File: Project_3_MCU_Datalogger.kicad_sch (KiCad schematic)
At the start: 25 parts, among them U1 24LC1025, U2 24LC1025, U3 DS1337S_, U4 ATMEGA328P-AU, Y1 Crystal, Y2 Crystal

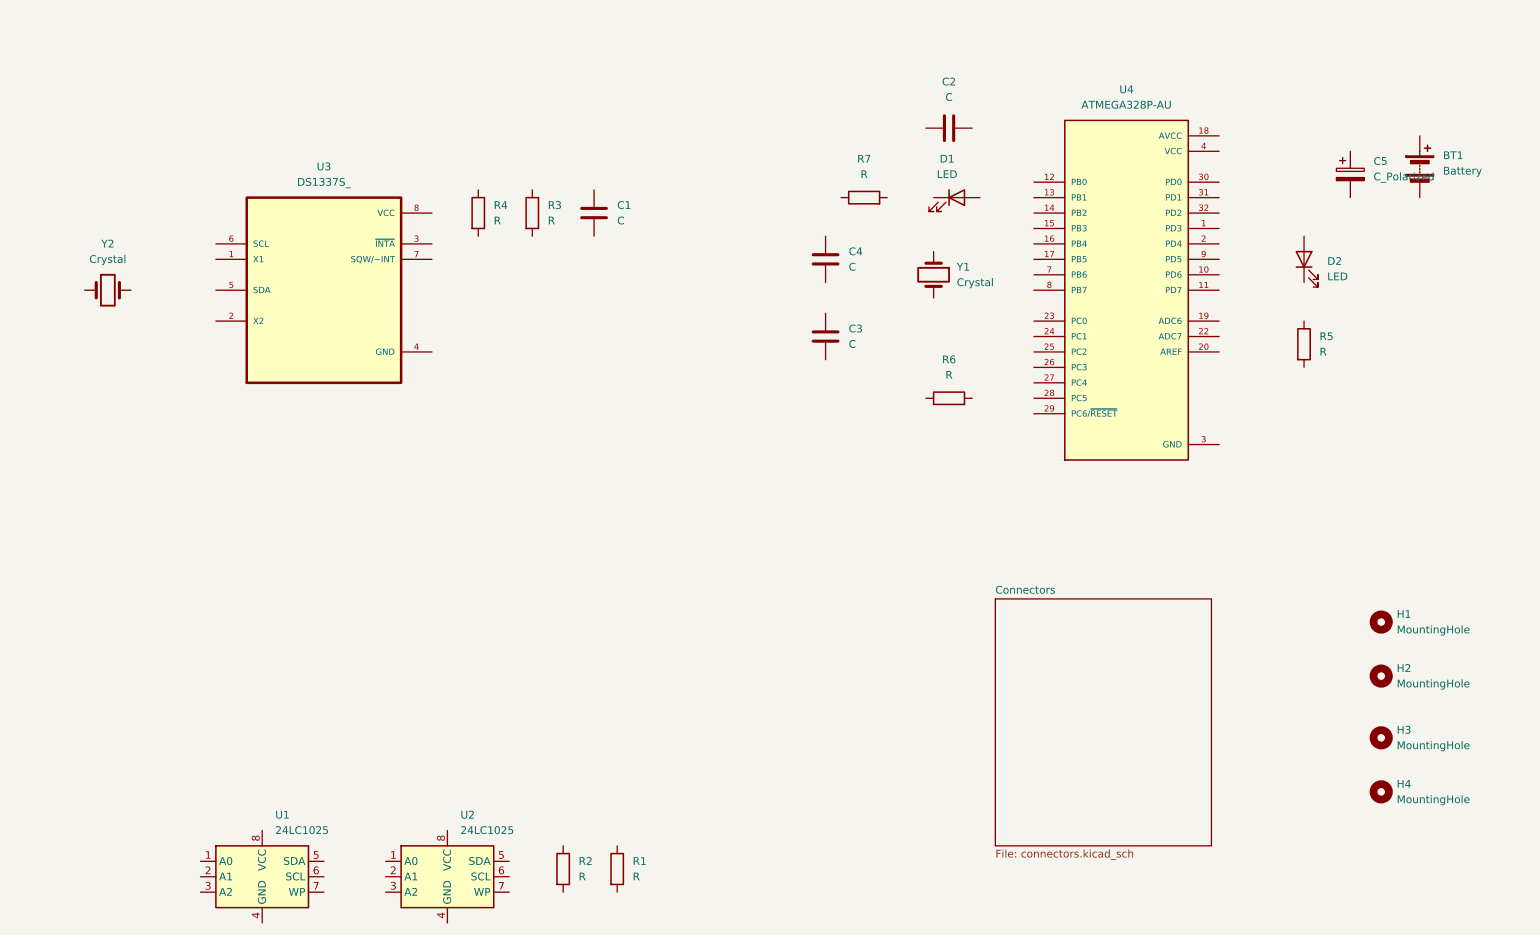
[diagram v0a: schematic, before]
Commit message: ajout des valeurs de composants
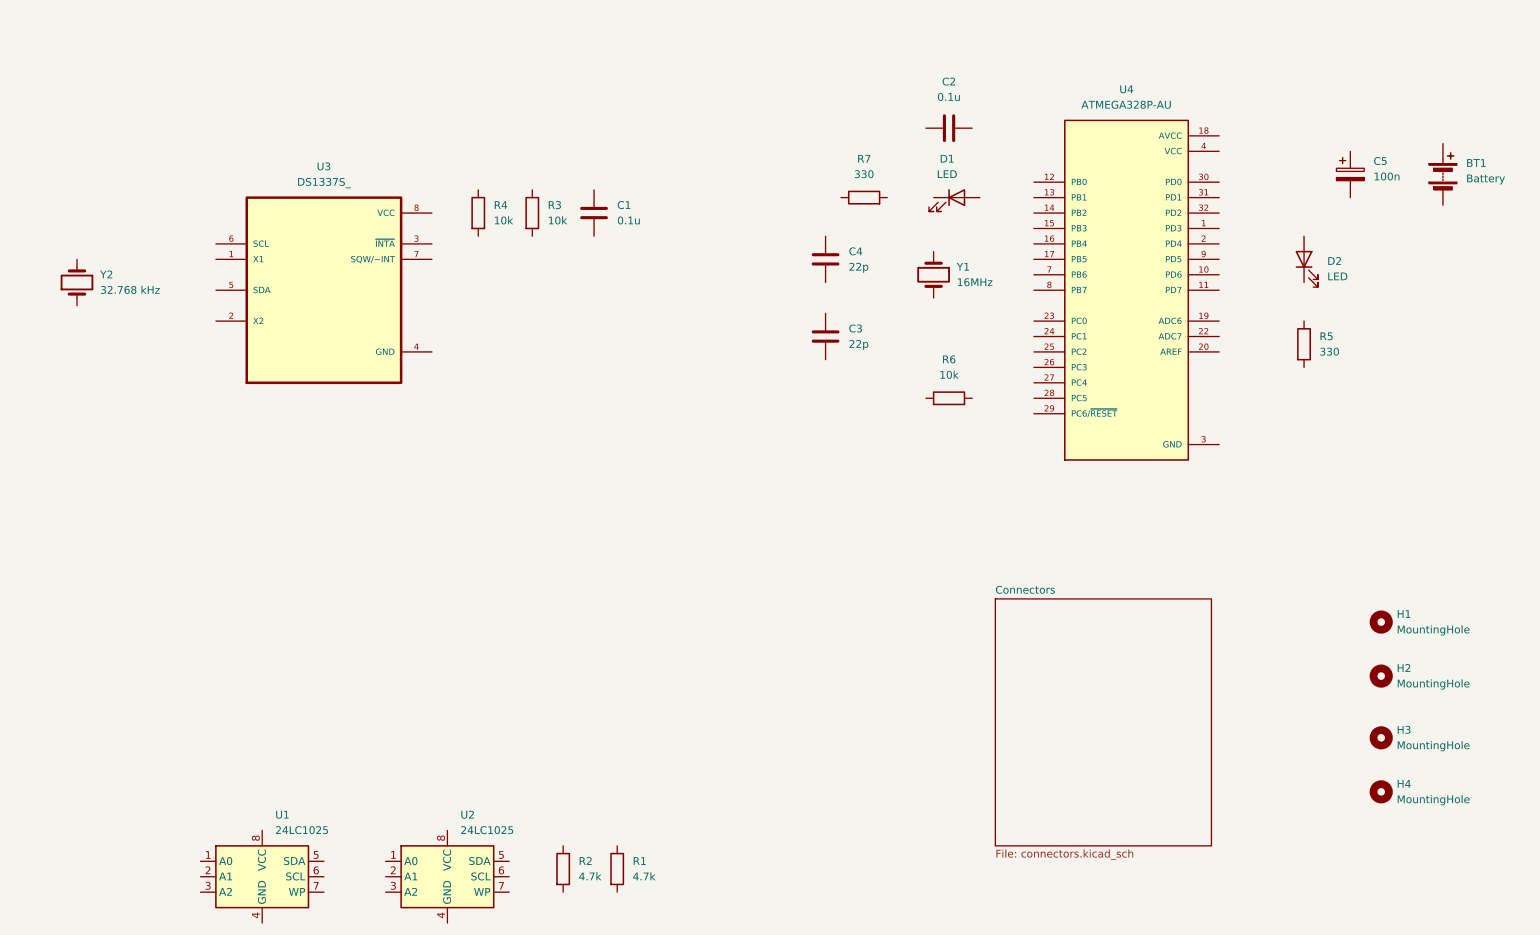
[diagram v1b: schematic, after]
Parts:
- C1, C2: value C -> 0.1u
- C3, C4: value C -> 22p
- C5: value C_Polarized -> 100n
- R1, R2: value R -> 4.7k
- R3, R4, R6: value R -> 10k
- R5, R7: value R -> 330
- Y1: value Crystal -> 16MHz
- Y2: value Crystal -> 32.768 kHz
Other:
- moved on the sheet: BT1, Y2
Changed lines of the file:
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@@
 			)
 		)
-		(property "Value" "Crystal"
+		(property "Value" "16MHz"
 			(at 180.34 66.0399 90)
 			(show_name no)
@@
 			)
 		)
-		(property "Value" "C"
+		(property "Value" "0.1u"
 			(at 124.46 55.8799 0)
 			(show_name no)
@@
 			)
 		)
-		(property "Value" "R"
+		(property "Value" "4.7k"
 			(at 118.11 163.8299 0)
 			(show_name no)
@@
 			)
 		)
-		(property "Value" "R"
+		(property "Value" "4.7k"
 			(at 127 163.8299 0)
 			(show_name no)
@@
 	(symbol
 		(lib_id "Device:Crystal")
-		(at 40.64 67.31 0)
+		(at 35.56 66.04 90)
 		(unit 1)
 		(body_style 1)
@@
 		(fields_autoplaced yes)
 		(property "Reference" "Y2"
-			(at 40.64 59.69 0)
-			(show_name no)
-			(do_not_autoplace no)
-			(effects
-				(font
-					(size 1.27 1.27)
-				)
-			)
-		)
-		(property "Value" "Crystal"
-			(at 40.64 62.23 0)
-			(show_name no)
-			(do_not_autoplace no)
-			(effects
-				(font
-					(size 1.27 1.27)
-				)
+			(at 39.37 64.7699 90)
+			(show_name no)
+			(do_not_autoplace no)
+			(effects
+				(font
+					(size 1.27 1.27)
+				)
+				(justify right)
+			)
+		)
+		(property "Value" "32.768 kHz"
+			(at 39.37 67.3099 90)
+			(show_name no)
+			(do_not_autoplace no)
+			(effects
+				(font
+					(size 1.27 1.27)
+				)
+				(justify right)
 			)
 		)
 		(property "Footprint" ""
-			(at 40.64 67.31 0)
+			(at 35.56 66.04 0)
 			(hide yes)
 			(show_name no)
@@
 		)
 		(property "Datasheet" ""
-			(at 40.64 67.31 0)
+			(at 35.56 66.04 0)
 			(hide yes)
 			(show_name no)
@@
 		)
 		(property "Description" "Two pin crystal"
-			(at 40.64 67.31 0)
-			(hide yes)
+			(at 35.56 66.04 0)
+			(hide yes)
+			(show_name no)
+			(do_not_autoplace no)
+			(effects
+				(font
+					(size 1.27 1.27)
+				)
+			)
+		)
+		(property "Purpose" ""
+			(at 35.56 66.04 0)
 			(show_name no)
 			(do_not_autoplace no)
@@
 			)
 		)
-		(property "Value" "R"
+		(property "Value" "10k"
 			(at 179.07 81.28 90)
 			(show_name no)
@@
 			)
 		)
-		(property "Value" "C"
+		(property "Value" "22p"
 			(at 162.56 76.1999 0)
 			(show_name no)
@@
 			)
 		)
-		(property "Value" "C"
+		(property "Value" "0.1u"
 			(at 179.07 35.56 90)
 			(show_name no)
@@
 			)
 		)
-		(property "Value" "C_Polarized"
+		(property "Value" "100n"
 			(at 248.92 48.6409 0)
 			(show_name no)
@@
 			)
 		)
-		(property "Value" "C"
+		(property "Value" "22p"
 			(at 162.56 63.4999 0)
 			(show_name no)
@@
 			)
 		)
-		(property "Value" "R"
+		(property "Value" "330"
 			(at 240.03 77.4699 0)
 			(show_name no)
@@
 	(symbol
 		(lib_id "Device:Battery")
-		(at 256.54 46.99 0)
+		(at 260.35 48.26 0)
 		(unit 1)
 		(body_style 1)
@@
 		(fields_autoplaced yes)
 		(property "Reference" "BT1"
-			(at 260.35 45.1484 0)
+			(at 264.16 46.4184 0)
 			(show_name no)
 			(do_not_autoplace no)
@@
 		)
 		(property "Value" "Battery"
-			(at 260.35 47.6884 0)
+			(at 264.16 48.9584 0)
 			(show_name no)
 			(do_not_autoplace no)
@@
 		)
 		(property "Footprint" ""
-			(at 256.54 45.466 90)
+			(at 260.35 46.736 90)
 			(hide yes)
 			(show_name no)
@@
 		)
 		(property "Datasheet" ""
-			(at 256.54 45.466 90)
+			(at 260.35 46.736 90)
 			(hide yes)
 			(show_name no)
@@
 		)
 		(property "Description" "Multiple-cell battery"
-			(at 256.54 46.99 0)
+			(at 260.35 48.26 0)
 			(hide yes)
 			(show_name no)
@@
 		)
 		(property "Sim.Device" "V"
-			(at 256.54 46.99 0)
+			(at 260.35 48.26 0)
 			(hide yes)
 			(show_name no)
@@
 		)
 		(property "Sim.Type" "DC"
-			(at 256.54 46.99 0)
+			(at 260.35 48.26 0)
 			(hide yes)
 			(show_name no)
@@
 		)
 		(property "Sim.Pins" "1=+ 2=-"
-			(at 256.54 46.99 0)
+			(at 260.35 48.26 0)
 			(hide yes)
 			(show_name no)
@@
 			)
 		)
-		(property "Value" "R"
+		(property "Value" "10k"
 			(at 113.03 55.8799 0)
 			(show_name no)
@@
 			)
 		)
-		(property "Value" "R"
+		(property "Value" "10k"
 			(at 104.14 55.8799 0)
 			(show_name no)
@@
 			)
 		)
+		(property "Purpose" ""
+			(at 101.6 54.61 0)
+			(show_name no)
+			(do_not_autoplace no)
+			(effects
+				(font
+					(size 1.27 1.27)
+				)
+			)
+		)
 		(pin "2"
 		)
@@
 			)
 		)
-		(property "Value" "R"
+		(property "Value" "330"
 			(at 165.1 48.26 90)
 			(show_name no)

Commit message: Association des empreintes aux composants
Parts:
- BT1: footprint (none) -> Connector_PinHeader_2.54mm:PinHeader_1x02_P2.54mm_Vertical
- C1, C2, C3, C4, C5: footprint (none) -> Capacitor_SMD:C_0805_2012Metric
- D1, D2: footprint (none) -> LED_SMD:LED_0805_2012Metric
- H1, H2, H3, H4: footprint (none) -> MountingHole:MountingHole_2.1mm
- R1, R2, R3, R4, R5, R6, R7: footprint (none) -> Resistor_SMD:R_0805_2012Metric
- U1, U2: footprint (none) -> Package_SO:SOIC-8_5.3x5.3mm_P1.27mm
- Y1, Y2: footprint (none) -> Crystal:Crystal_SMD_5032-2Pin_5.0x3.2mm_HandSoldering
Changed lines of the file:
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@@
 			)
 		)
-		(property "Footprint" ""
+		(property "Footprint" "Crystal:Crystal_SMD_5032-2Pin_5.0x3.2mm_HandSoldering"
 			(at 176.53 64.77 0)
 			(hide yes)
@@
 			)
 		)
-		(property "Footprint" ""
+		(property "Footprint" "LED_SMD:LED_0805_2012Metric"
 			(at 180.34 52.07 0)
 			(hide yes)
@@
 			)
 		)
-		(property "Footprint" ""
+		(property "Footprint" "Capacitor_SMD:C_0805_2012Metric"
 			(at 121.6152 58.42 0)
 			(hide yes)
@@
 			)
 		)
-		(property "Footprint" ""
+		(property "Footprint" "Package_SO:SOIC-8_5.3x5.3mm_P1.27mm"
 			(at 96.52 163.83 0)
 			(hide yes)
@@
 			)
 		)
-		(property "Footprint" ""
+		(property "Footprint" "MountingHole:MountingHole_2.1mm"
 			(at 250.19 149.86 0)
 			(hide yes)
@@
 			)
 		)
-		(property "Footprint" ""
+		(property "Footprint" "MountingHole:MountingHole_2.1mm"
 			(at 250.19 130.81 0)
 			(hide yes)
@@
 			)
 		)
-		(property "Footprint" ""
+		(property "Footprint" "Resistor_SMD:R_0805_2012Metric"
 			(at 113.792 162.56 90)
 			(hide yes)
@@
 			)
 		)
-		(property "Footprint" ""
+		(property "Footprint" "Resistor_SMD:R_0805_2012Metric"
 			(at 122.682 162.56 90)
 			(hide yes)
@@
 			)
 		)
-		(property "Footprint" ""
+		(property "Footprint" "Crystal:Crystal_SMD_5032-2Pin_5.0x3.2mm_HandSoldering"
 			(at 35.56 66.04 0)
 			(hide yes)
@@
 			)
 		)
-		(property "Footprint" ""
+		(property "Footprint" "Resistor_SMD:R_0805_2012Metric"
 			(at 179.07 86.868 90)
 			(hide yes)
@@
 			)
 		)
-		(property "Footprint" ""
+		(property "Footprint" "Capacitor_SMD:C_0805_2012Metric"
 			(at 159.7152 78.74 0)
 			(hide yes)
@@
 			)
 		)
-		(property "Footprint" ""
+		(property "Footprint" "LED_SMD:LED_0805_2012Metric"
 			(at 237.49 62.23 0)
 			(hide yes)
@@
 			)
 		)
-		(property "Footprint" ""
+		(property "Footprint" "Capacitor_SMD:C_0805_2012Metric"
 			(at 182.88 39.6748 0)
 			(hide yes)
@@
 			)
 		)
-		(property "Footprint" ""
+		(property "Footprint" "Capacitor_SMD:C_0805_2012Metric"
 			(at 246.0752 52.07 0)
 			(hide yes)
@@
 			)
 		)
-		(property "Footprint" ""
+		(property "Footprint" "MountingHole:MountingHole_2.1mm"
 			(at 250.19 121.92 0)
 			(hide yes)
@@
 			)
 		)
-		(property "Footprint" ""
+		(property "Footprint" "Capacitor_SMD:C_0805_2012Metric"
 			(at 157.7848 58.42 0)
 			(hide yes)
@@
 			)
 		)
-		(property "Footprint" ""
+		(property "Footprint" "Resistor_SMD:R_0805_2012Metric"
 			(at 235.712 76.2 90)
 			(hide yes)
@@
 			)
 		)
-		(property "Footprint" ""
+		(property "Footprint" "Connector_PinHeader_2.54mm:PinHeader_1x02_P2.54mm_Vertical"
 			(at 260.35 46.736 90)
 			(hide yes)
@@
 			)
 		)
-		(property "Footprint" ""
+		(property "Footprint" "Resistor_SMD:R_0805_2012Metric"
 			(at 108.712 54.61 90)
 			(hide yes)
@@
 			)
 		)
-		(property "Footprint" ""
+		(property "Footprint" "Resistor_SMD:R_0805_2012Metric"
 			(at 99.822 54.61 90)
 			(hide yes)
@@
 			)
 		)
-		(property "Footprint" ""
+		(property "Footprint" "MountingHole:MountingHole_2.1mm"
 			(at 250.19 140.97 0)
 			(hide yes)
@@
 			)
 		)
-		(property "Footprint" ""
+		(property "Footprint" "Package_SO:SOIC-8_5.3x5.3mm_P1.27mm"
 			(at 66.04 163.83 0)
 			(hide yes)
@@
 			)
 		)
-		(property "Footprint" ""
+		(property "Footprint" "Resistor_SMD:R_0805_2012Metric"
 			(at 165.1 53.848 90)
 			(hide yes)

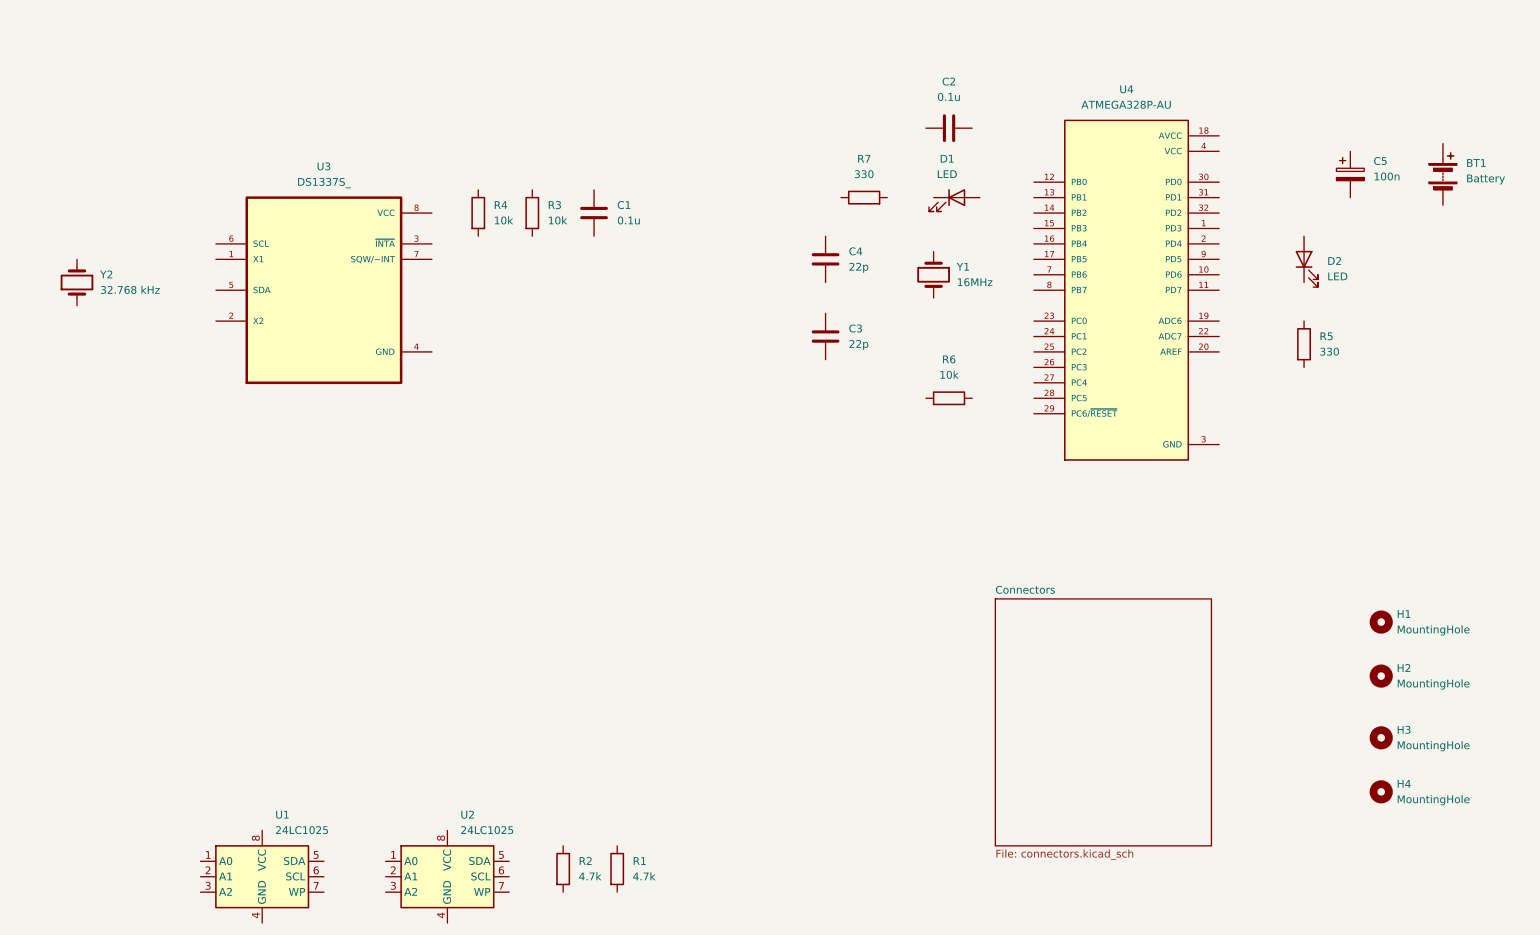
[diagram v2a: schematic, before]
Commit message: wiring of sheet 1
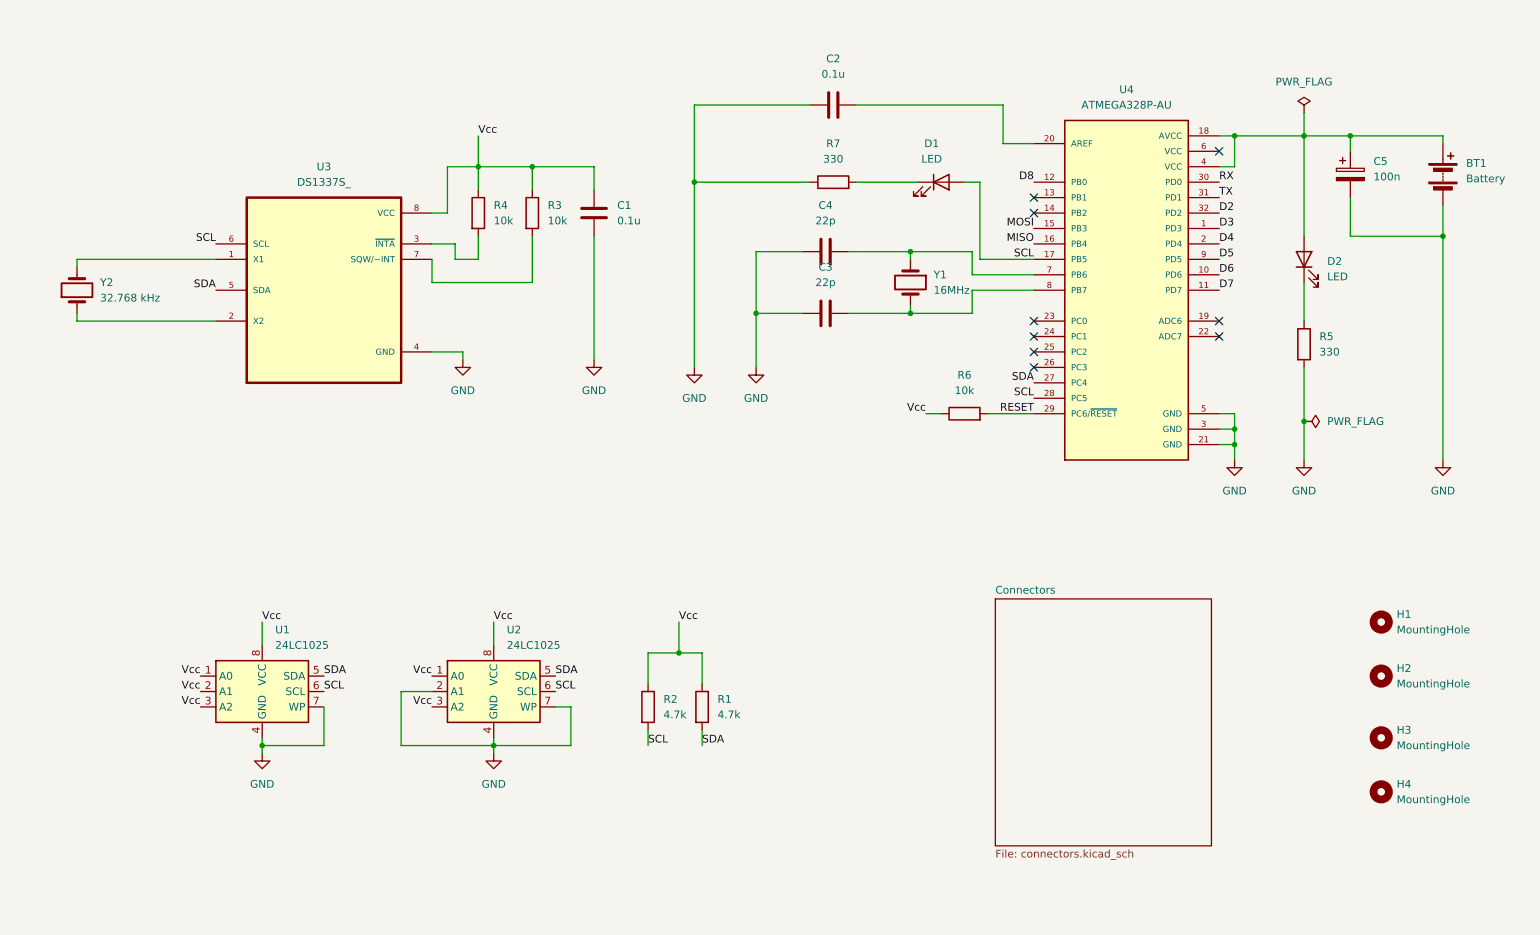
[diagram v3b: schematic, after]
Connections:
- net GND: now also BT1.2 (-), C1.2, C2.1, C3.1, C4.2, C5.2, R5.2, R7.1, U1.4 (GND), U1.7 (WP), U2.2 (A1), U2.4 (GND), U2.7 (WP), U3.4 (GND)
- net at Y1.1: now also C4.1, U4.7 (PB6)
- net at Y1.2: now also C3.2, U4.8 (PB7)
- net at D1.1 (K): now also R7.2
- net SCL: now reaches D1.2 (A)
- net SCL: now also R2.2, U1.6 (SCL), U2.6 (SCL), U3.6 (SCL), U4.17 (PB5), U4.28 (PC5)
- net Vcc: now reaches C1.1
- net Vcc: now also R1.1, R2.1, R3.1, R4.1, R6.1, U1.1 (A0), U1.2 (A1), U1.3 (A2), U1.8 (VCC), U2.1 (A0), U2.3 (A2), U2.8 (VCC), U3.8 (VCC)
- net at U3.1 (X1): now also Y2.2
- net at U3.2 (X2): now also Y2.1
- net at U3.3 (~{INTA}): now also R4.2
- net SDA: now reaches U3.5 (SDA)
- net SDA: now also R1.2, U1.5 (SDA), U2.5 (SDA), U4.27 (PC4)
- net at U3.7 (SQW/~INT): now also R3.2
- net D3: now reaches U4.1 (PD3)
- net D6: now reaches U4.10 (PD6)
- net D7: now reaches U4.11 (PD7)
- net D8: now reaches U4.12 (PB0)
- net MOSI: now reaches U4.15 (PB3)
- net MISO: now reaches U4.16 (PB4)
- net at U4.18 (AVCC): now also BT1.1 (+), C5.1, D2.2 (A), U4.4 (VCC)
- net D4: now reaches U4.2 (PD4)
- net at U4.20 (AREF): now also C2.2
- net RESET: now reaches U4.29 (PC6/~{RESET})
- net RESET: now also R6.2
- net RX: now reaches U4.30 (PD0)
- net TX: now reaches U4.31 (PD1)
- net D2: now reaches U4.32 (PD2)
- net D5: now reaches U4.9 (PD5)
- net at D2.1 (K): now also R5.1
- net VCC: no longer names the net of U4.6 (VCC)
- net VCC: no longer U4.4 (VCC)
- no-connect marks 0 -> 9
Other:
- moved on the sheet: C2, C3, C4, D1, R1, R2, R6, R7, U1, U2, Y1, Y2

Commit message: wiring sheet 2, wiring done
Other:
- sheet Connectors ports: added D2, D3, D4, D5, D6, D7, D8, GND, MISO, MOSI, RESET, RX, SCL, SDA, TX, Vcc; removed none
